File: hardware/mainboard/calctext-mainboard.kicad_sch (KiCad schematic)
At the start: 25 parts, among them J1 LCD_FFC, SW1 Keypad_Contact, U1 Wio-E5-LE, U2 TPS61299

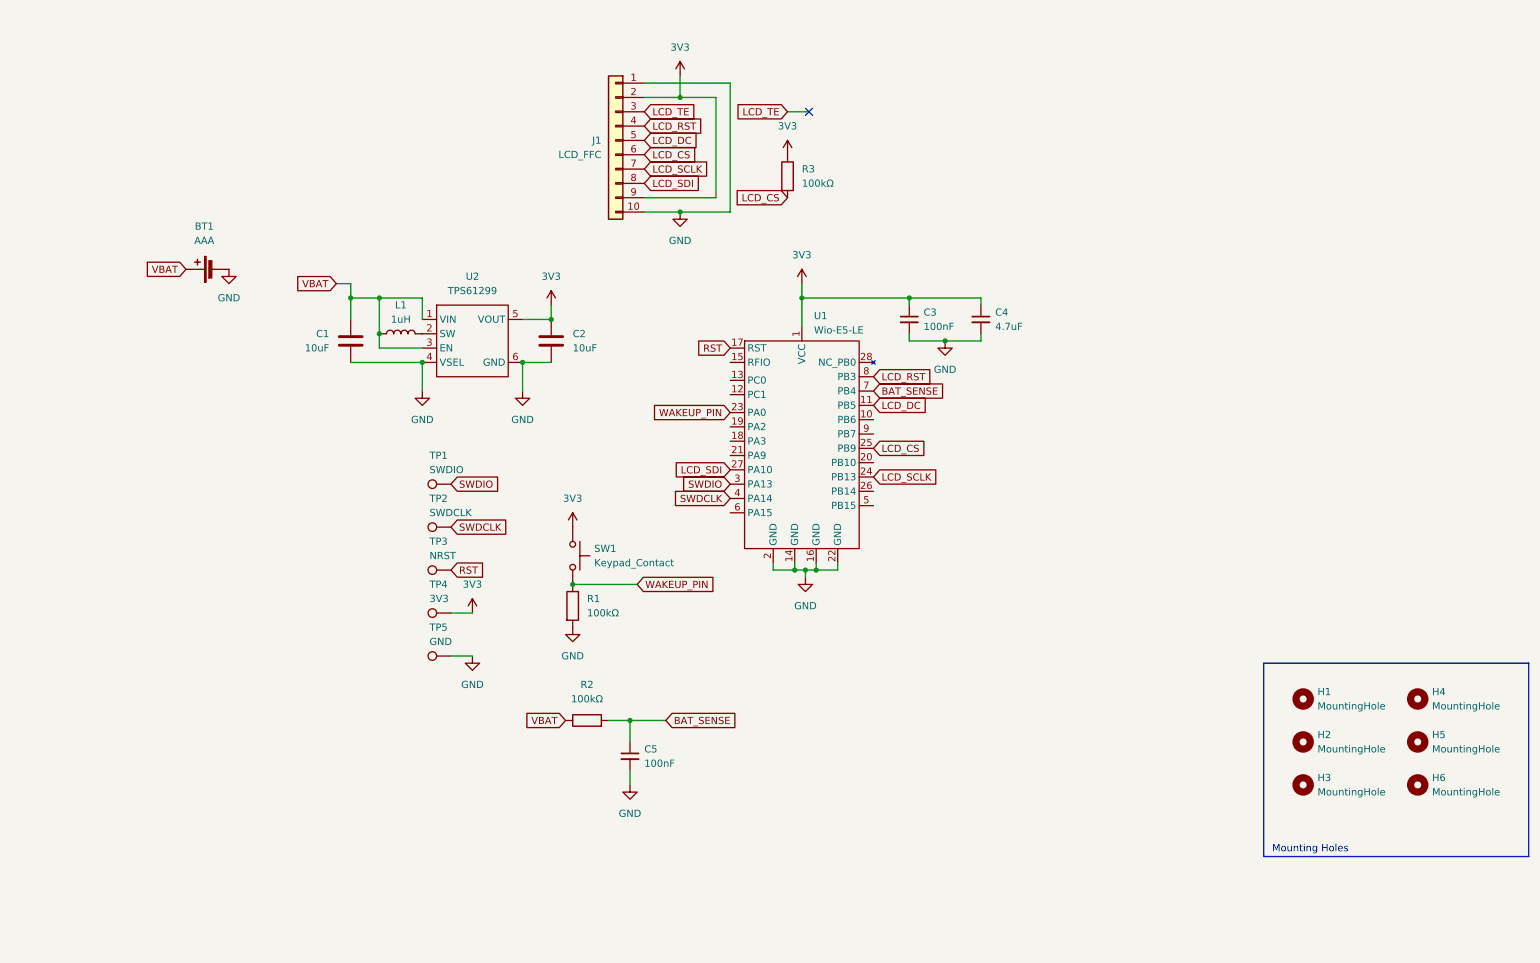
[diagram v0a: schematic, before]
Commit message: Add keypad I/O expander interface
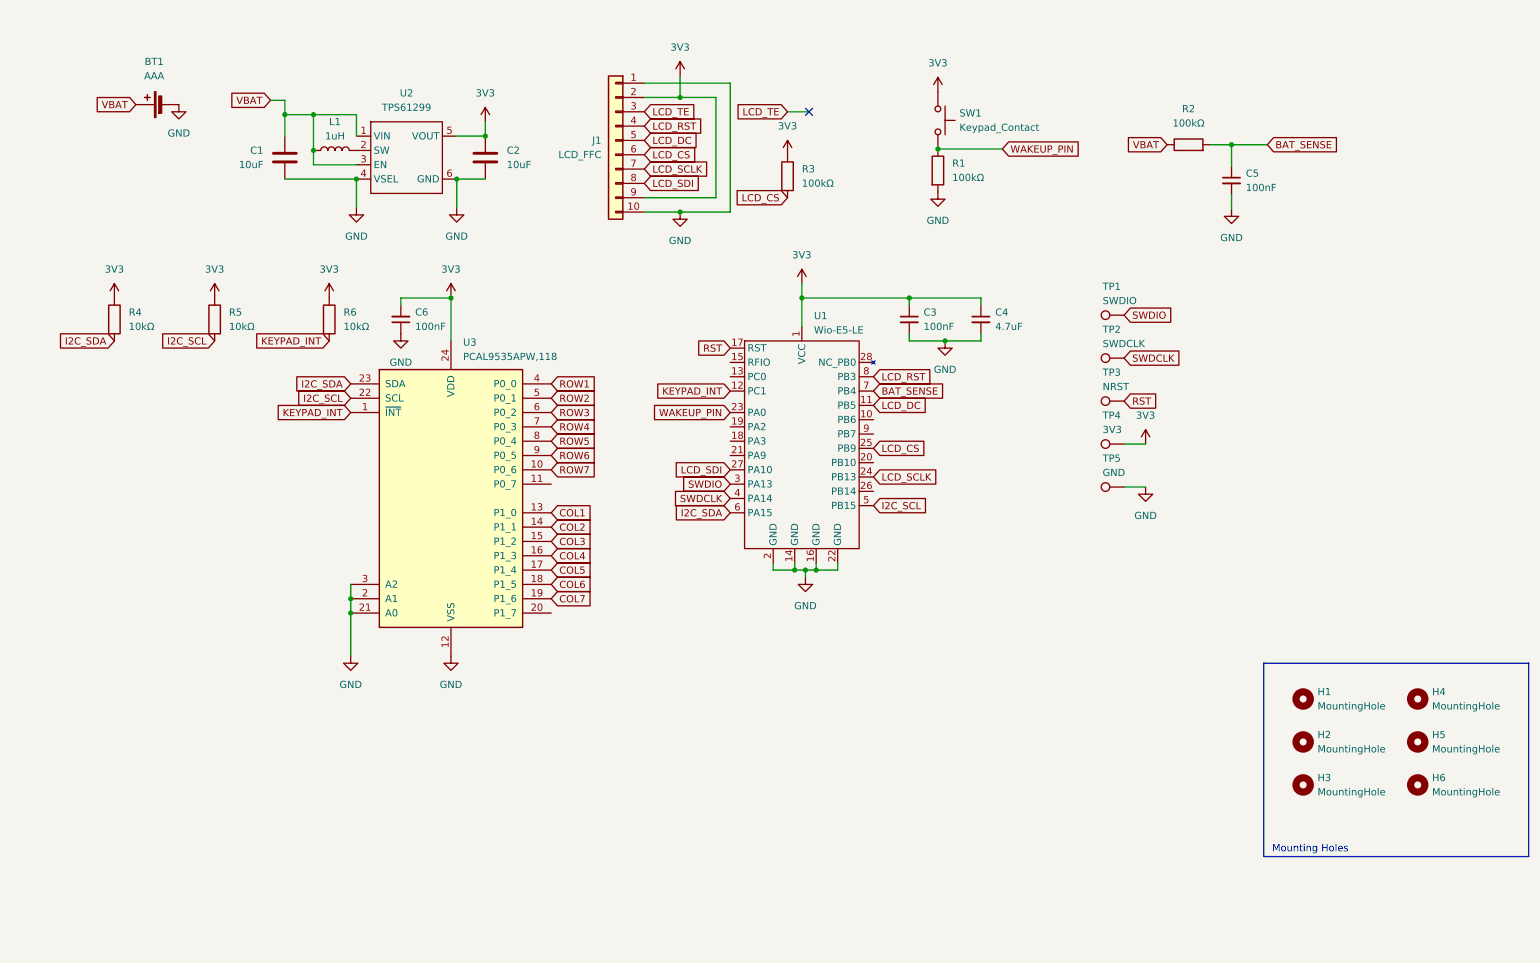
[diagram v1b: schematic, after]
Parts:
- added C6: 100nF, symbol Device:C_Small
- added R4, R5, R6: 10kΩ, symbol Device:R
- added U3: PCAL9535APW,118, Package_SO:TSSOP-24_4.4x7.8mm_P0.65mm, symbol CalcText:PCAL9535APW
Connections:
- net 3V3: now also C6.2, R4.1, R5.1, R6.1, U3.24 (VDD)
- net GND: now also C6.1, U3.12 (VSS), U3.2 (A1), U3.21 (A0), U3.3 (A2)
- net KEYPAD_INT: now reaches U1.12 (PC1)
- net KEYPAD_INT: now also R6.2, U3.1 (~{INT})
- net I2C_SCL: now reaches U1.5 (PB15)
- net I2C_SCL: now also R5.2, U3.22 (SCL)
- net I2C_SDA: now reaches U1.6 (PA15)
- net I2C_SDA: now also R4.2, U3.23 (SDA)
- new net COL1: U3.13 (P1_0)
- new net COL2: U3.14 (P1_1)
- new net COL3: U3.15 (P1_2)
- new net COL4: U3.16 (P1_3)
- new net COL5: U3.17 (P1_4)
- new net COL6: U3.18 (P1_5)
- new net COL7: U3.19 (P1_6)
- new net ROW1: U3.4 (P0_0)
- new net ROW2: U3.5 (P0_1)
- new net ROW3: U3.6 (P0_2)
- new net ROW4: U3.7 (P0_3)
- new net ROW5: U3.8 (P0_4)
- new net ROW6: U3.9 (P0_5)
- new net ROW7: U3.10 (P0_6)
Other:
- moved on the sheet: BT1, C1, C2, C5, L1, R1, R2, SW1, TP1, TP2, TP3, TP4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

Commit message: Add 7x7 keypad matrix schematic
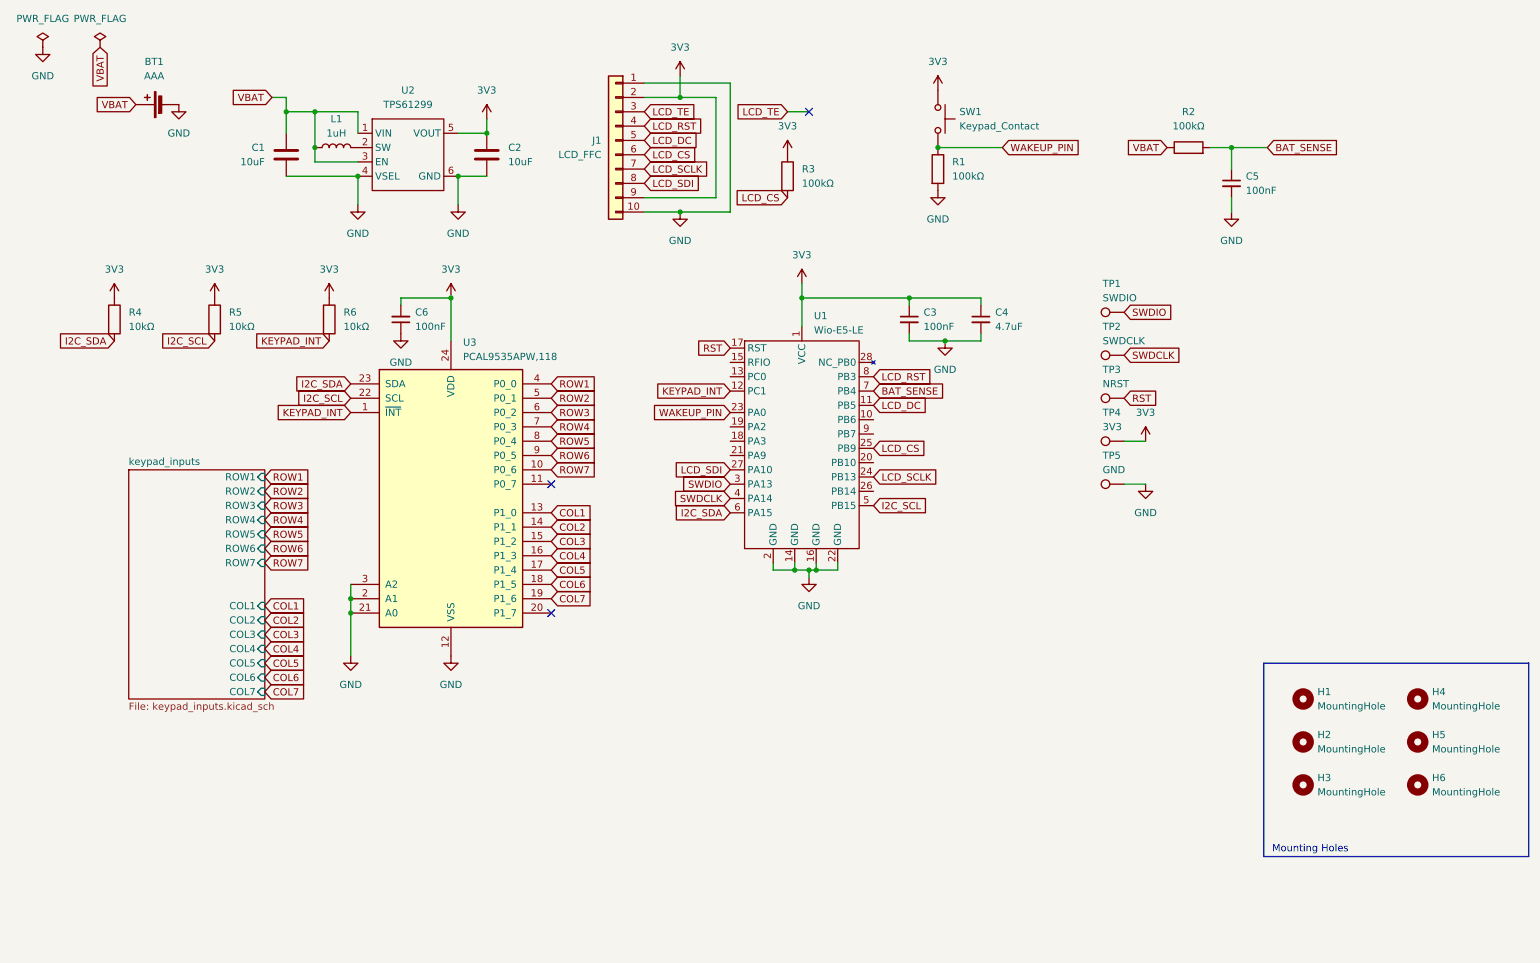
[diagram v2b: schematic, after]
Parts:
- SW1: footprint (none) -> CalcText:keypad_trace_button
- U1: footprint Wio-E5-LE:Wio-E5-LE -> CalcText:Wio-E5-LE
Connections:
- no-connect marks 1 -> 3
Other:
- added sheet keypad_inputs (keypad_inputs.kicad_sch)
- moved on the sheet: C1, C2, C5, L1, R2, TP1, TP2, TP3, TP4, TP5, U2

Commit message: Complete mainboard RF and debug interfaces
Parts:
- removed BT1: AAA, symbol Device:Battery_Cell
- added AE1: Antenna, CalcText:Wire_Antenna_PTH, symbol Device:Antenna
- added C7, C8: DNP, Capacitor_SMD:C_0402_1005Metric, symbol Device:C
- added J2: J_BAT+, CalcText:Wire_Solder_PTH, symbol Connector_Generic:Conn_01x01
- added J3: J_BAT-, CalcText:Wire_Solder_PTH, symbol Connector_Generic:Conn_01x01
- added L2: 0R, Inductor_SMD:L_0402_1005Metric, symbol Device:L
- added TP4: SWO, TestPoint:TestPoint_Pad_D2.0mm, symbol Connector:TestPoint
- C1, C2: footprint (none) -> Capacitor_SMD:C_0805_2012Metric_Pad1.18x1.45mm_HandSolder
- C3, C4, C5, C6: footprint (none) -> Capacitor_SMD:C_0603_1608Metric_Pad1.08x0.95mm_HandSolder
- J1: footprint (none) -> CalcText_Shared:Hirose_FH34SRJ-10S-0.5SH
- L1: footprint (none) -> Inductor_SMD:L_0805_2012Metric_Pad1.15x1.40mm_HandSolder
- R1, R2, R3, R4, R5, R6: footprint (none) -> Resistor_SMD:R_0603_1608Metric_Pad0.98x0.95mm_HandSolder
- SW1: footprint CalcText:keypad_trace_button -> (none)
- TP1, TP2, TP3: footprint (none) -> TestPoint:TestPoint_Pad_D2.0mm
- TP5: renamed from TP4; footprint (none) -> TestPoint:TestPoint_Pad_D2.0mm
- TP6: renamed from TP5; footprint (none) -> TestPoint:TestPoint_Pad_D2.0mm
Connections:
- net GND: now also C7.2, C8.2, J3.1 (Pin_1)
- net LCD_RST: now also U1.13 (PC0); no longer U1.8 (PB3)
- net VBAT: now also J2.1 (Pin_1)
- net WIO_RFIO: now reaches U1.15 (RFIO)
- net WIO_RFIO: now also C7.1, L2.1
- new net ANT_868: AE1.1 (A), C8.1, L2.2
- new net SWO: TP4.1, U1.8 (PB3)
- no-connect marks 3 -> 10
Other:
- moved on the sheet: TP5, TP6

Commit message: Polish mainboard schematic presentation
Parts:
- U1: footprint CalcText:Wio-E5-LE -> Wio-E5-LE:Wio-E5-LE
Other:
- note added: "Battery sense circuit"
- note added: "Boost converter"
- note added: "GPIO expander"
- note added: "GPIO expander pull-ups"
- note added: "Keypad matrix"
- note added: "LCD FFC connector"
- note added: "MCU and LoRa modem"
- note added: "Mounting holes"
- note added: "Power input"
- note added: "RF matching network"
- note added: "SWD user interface"
- note added: "Wake-up circuit"
- note removed: "Mounting Holes"
- moved on the sheet: AE1, C1, C2, C3, C4, C5, C6, C7, C8, H1, H2, H3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

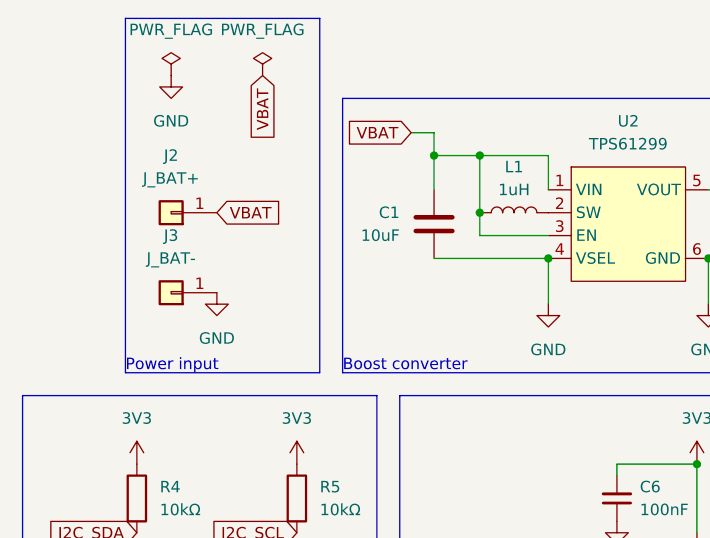
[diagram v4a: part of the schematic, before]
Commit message: Update mainboard power inductor
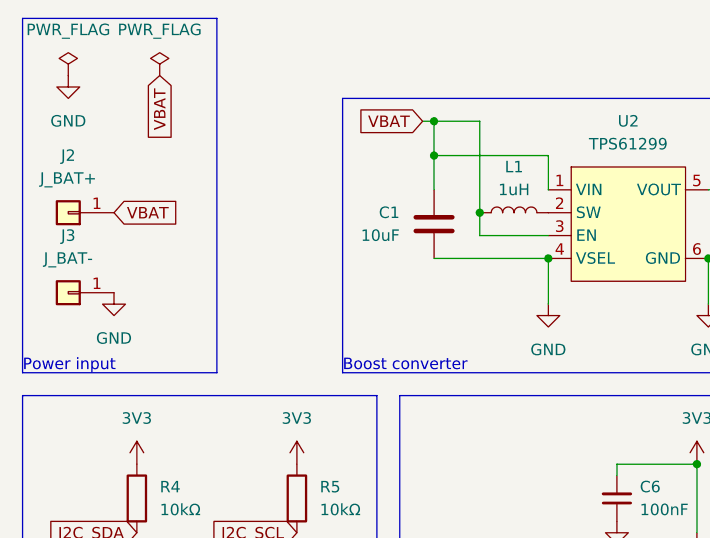
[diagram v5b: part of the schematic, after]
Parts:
- L1: footprint Inductor_SMD:L_0805_2012Metric_Pad1.15x1.40mm_HandSolder -> CalcText:L_INPAQ_WIP252010; DCR_Max  (none) -> 54mΩ; Irms  (none) -> 2.7A min / 3.0A typ; Isat  (none) -> 3.15A min / 3.5A typ; MPN (none) -> WIP252010P-1R0ML; Manufacturer (none) -> Manufacturer
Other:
- moved on the sheet: J2, J3

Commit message: Refine hardware for fabrication and procurement
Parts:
- AE1, J2, J3, SW1, TP1, TP2, TP3, TP4, TP5, TP6: now left out of the parts list
- C1, C2: MPN (none) -> CL21B106KOQNNNE; Manufacturer (none) -> Samsung Electro-Mechanics
- C3, C5, C6: MPN (none) -> C0603C104K5RACTU; Manufacturer (none) -> KEMET
- C4: MPN (none) -> CL10B475KQ8NNNC; Manufacturer (none) -> Samsung Electro-Mechanics
- J1: value LCD_FFC -> FH34SRJ-10S-0.5SH; MPN (none) -> FH34SRJ-10S-0.5SH(99); Manufacturer (none) -> Hirose Electric
- L1: DCR_Max (none) -> 54mΩ; DCR_Max  54mΩ -> (none); Irms (none) -> 2.7A min / 3.0A typ; Irms  2.7A min / 3.0A typ -> (none); Isat (none) -> 3.15A min / 3.5A typ; Isat  3.15A min / 3.5A typ -> (none); Manufacturer Manufacturer -> INPAQ
- L2: MPN (none) -> RC0402JR-070RL; Manufacturer (none) -> YAGEO
- R1, R2, R3: MPN (none) -> RMCF0603FT100K; Manufacturer (none) -> Stackpole Electronics
- R4, R5, R6: MPN (none) -> RC0603FR-0710KL; Manufacturer (none) -> YAGEO
- U1: footprint Wio-E5-LE:Wio-E5-LE -> CalcText:Wio-E5-LE; MPN (none) -> Wio-E5-LE; Manufacturer (none) -> Seeed Studio; Supplier (none) -> Seeed Studio; Supplier SKU (none) -> 114993120
- U2: MPN (none) -> TPS61299DRLR; Manufacturer (none) -> Texas Instruments
- U3: MPN (none) -> PCAL9535APW,118; Manufacturer (none) -> NXP Semiconductors
